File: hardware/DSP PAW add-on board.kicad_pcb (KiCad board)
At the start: 2 copper layers, 63 x 53.5 mm, 75 parts, among them J1 AudioJack2_Ground, J3 Conn_01x02, J4 Conn_02x03_Odd_Even, J5 AudioJack2_Ground, J7 AudioJack2_Ground, J8 USB_B_Micro, U1 TLV9162, U2 OPA1678, U3 MAX6106, U4 LM27761

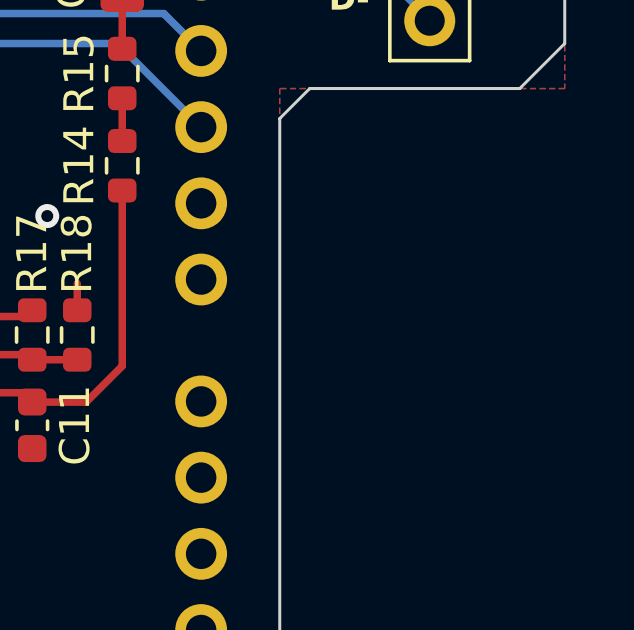
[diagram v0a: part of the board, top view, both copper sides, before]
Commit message: wip: schematic fixes based on testing
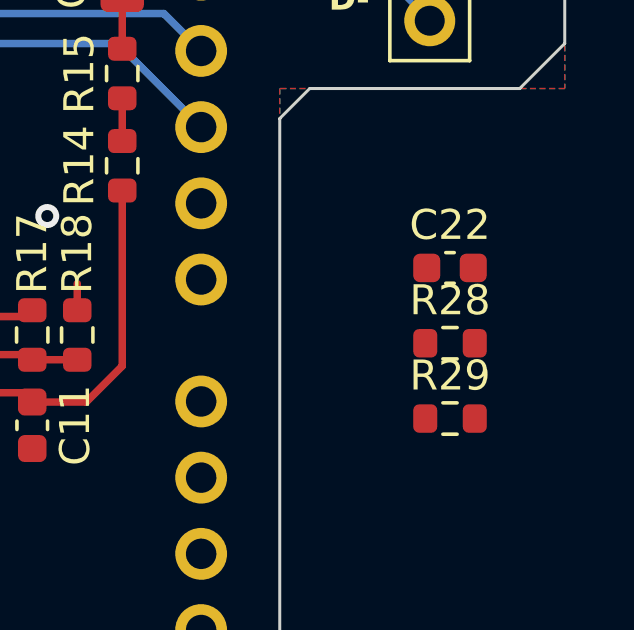
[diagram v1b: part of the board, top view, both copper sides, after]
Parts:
- added C22: 100p, Capacitor_SMD:C_0603_1608Metric, F.Cu at (179.2, 97.5)
- added R28: 100k, Resistor_SMD:R_0603_1608Metric, F.Cu at (179.2, 100.0)
- added R29: 100k, Resistor_SMD:R_0603_1608Metric, F.Cu at (179.2, 102.5)
- D1, D2, D3: value ESD5Zxx -> ESD5Z2.5T1G
- R1: value 9.09k -> 7.5k/0.1%
- R12, R13, R17, R18: value 2.49k -> 2.49k/0.1%
- R14, R8: value 22.1k -> 22.1k/0.1%
- R15, R9: value 6.81k -> 6.81k/0.1%
- R19: value 174k -> 174k/1%
- R21: value 56k -> 56k/1%
- R3: value 9.09k -> 9.09k/0.1%
- R4: value 6.34k -> 6.34k/0.1%
- R5: value 20k -> 10k/0.1%
- R7: value 10k/0.1% -> 30k/0.1%
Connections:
- net PC10/LED_R renamed LED_B
- net PC11/LED_G renamed LED_R
- net PC12/LED_B renamed LED_G
- A2 pad 5V1: +5VD -> VBUS
- A2 pad VIN: VBUS -> unconnected-(A2-PadVIN)
- C13 pad 1: +5VD -> VBUS
- C5 pad 2: Net-(U2A-+) -> Net-(C5-Pad2)
- C9 pad 2: Net-(U2B-+) -> Net-(C9-Pad2)
- L1 pad 1: +5VD -> VBUS
- R14 pad 2: Net-(R14-Pad2) -> Net-(C9-Pad2)
- R15 pad 1: Net-(R14-Pad2) -> Net-(C9-Pad2)
- R8 pad 2: Net-(R8-Pad2) -> Net-(C5-Pad2)
- R9 pad 1: Net-(R8-Pad2) -> Net-(C5-Pad2)
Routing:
- net Net-(R8-Pad2): track 1.50 -> 0.00 mm
- net Net-(C5-Pad2): track 0.00 -> 1.50 mm
- net Net-(R14-Pad2): track 1.42 -> 0.00 mm
- net Net-(C9-Pad2): track 0.00 -> 1.42 mm
- added copper zone on F.Cu, net VBUS
- removed copper zone on F.Cu, net +5VD

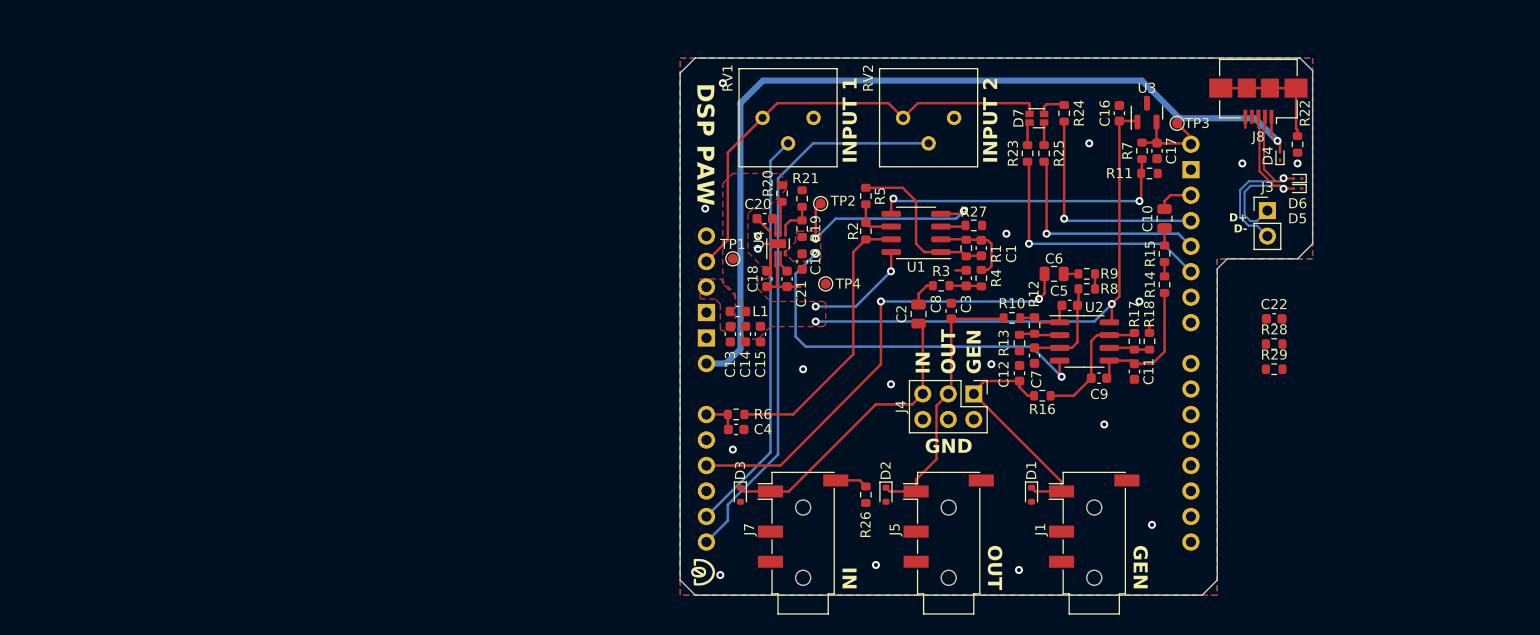
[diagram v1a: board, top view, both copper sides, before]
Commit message: use nucleo 3.3v vdda; add 2nd low-pass stage to input
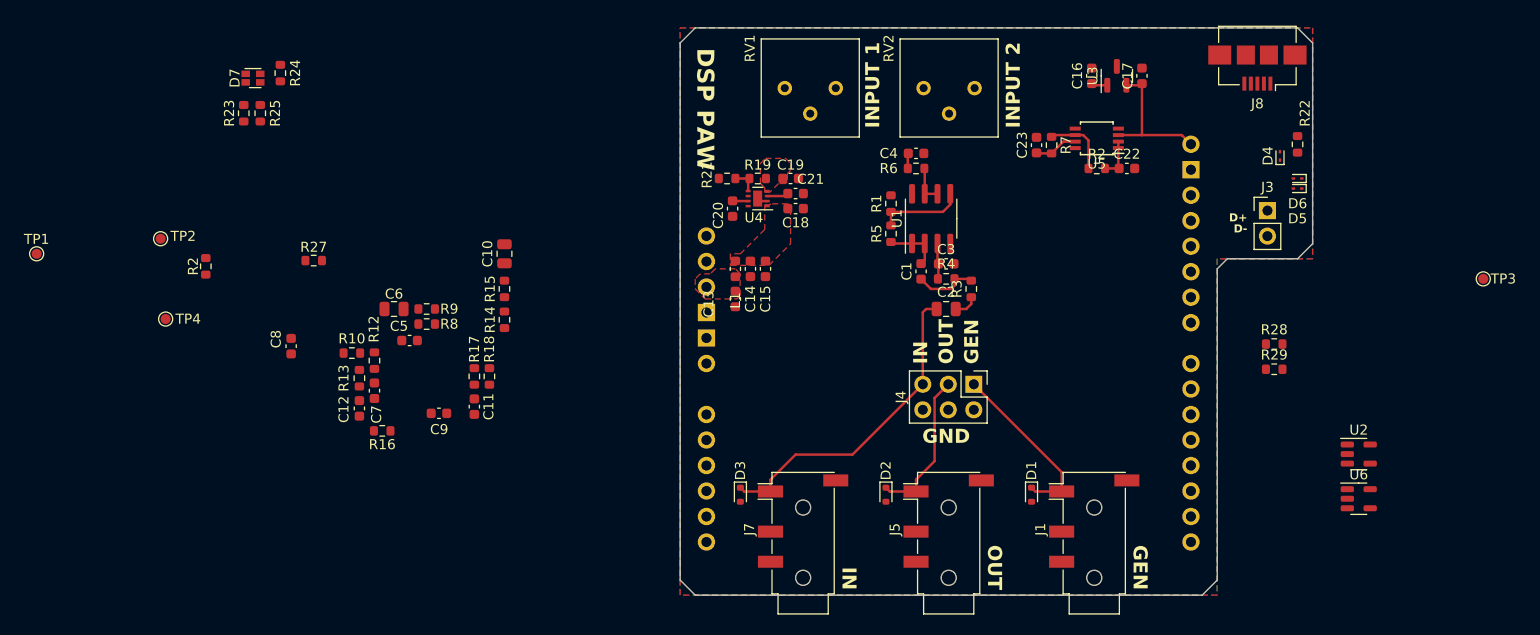
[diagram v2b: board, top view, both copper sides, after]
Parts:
- removed R11: 10k/0.1%, Resistor_SMD:R_0603_1608Metric
- removed R20, R26: 0, Resistor_SMD:R_0603_1608Metric
- added C23: 1u, Capacitor_SMD:C_0603_1608Metric, F.Cu at (155.5, 80.2)
- added R2: 10k/0.1%, Resistor_SMD:R_0603_1608Metric, F.Cu at (161.5, 82.5)
- added U5: OPA2310, Package_SO:TSSOP-8_3x3mm_P0.65mm, F.Cu at (161.5, 79.5)
- added U6: OPA1677, Package_TO_SOT_SMD:SOT-23-5, F.Cu at (187.6, 115.4)
- C1: value 100p -> 140p
- C22: value 100p -> 1u
- C3: value 274p -> 100p
- R1: value 7.5k/0.1% -> 10k/0.1%
- R3: value 9.09k/0.1% -> 8.45k/0.1%
- R4: value 6.34k/0.1% -> 13.2k/0.1%
- R7: value 30k/0.1% -> 10k/0.1%
- U2: value OPA1678 -> OPA1677; footprint Package_SO:SOIC-8_3.9x4.9mm_P1.27mm -> Package_TO_SOT_SMD:SOT-23-5
- U3: value MAX6106 -> REF3033
- moved D7 78.2 mm to (77.5, 73.5)
- moved R24 78.2 mm to (80.2, 73.0)
- moved R25 78.2 mm to (78.2, 77.0)
- moved R23 78.2 mm to (76.5, 77.0)
- moved TP1 69.4 mm to (55.9, 91.0)
- moved C12 65.8 mm to (88.0, 106.4)
- moved C5 65.8 mm to (93.0, 99.6)
- moved C7 65.8 mm to (89.5, 104.6)
- moved R10 65.8 mm to (87.3, 100.9)
- moved R12 65.8 mm to (89.5, 101.6)
- moved R13 65.8 mm to (88.0, 103.4)
- moved C10 65.8 mm to (102.5, 91.0)
- moved C11 65.8 mm to (99.5, 106.2)
- moved C6 65.8 mm to (91.5, 96.5)
- moved C8 65.8 mm to (81.2, 100.2)
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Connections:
- C1 pad 1: Net-(U1A--) -> Net-(C1-Pad1)
- C1 pad 2: Net-(C1-Pad2) -> Net-(U1A--)
- C11 pad 1: Net-(U2B-+) -> Net-(U6-+)
- C22 pad 1: Net-(U1B--) -> +3V3
- C22 pad 2: Net-(C22-Pad2) -> GND
- C3 pad 1: Net-(C3-Pad1) -> Net-(U1A-+)
- J7 pad S: Net-(J7-PadS) -> GND
- J8 pad 6: Net-(J8-Shield) -> GND
- R1 pad 1: Net-(U1A--) -> Net-(U1B-+)
- R1 pad 2: Net-(C1-Pad2) -> +3V3
- R12 pad 2: Net-(U2A--) -> Net-(U2--)
- R13 pad 1: Net-(U2A--) -> Net-(U2--)
- R14 pad 1: Net-(U2B-+) -> Net-(U6-+)
- R17 pad 2: Net-(U2B--) -> Net-(U6--)
- R18 pad 1: Net-(U2B--) -> Net-(U6--)
- R3 pad 2: Net-(C3-Pad1) -> Net-(C1-Pad1)
- R4 pad 1: Net-(C3-Pad1) -> Net-(C1-Pad1)
- R4 pad 2: Net-(U1A--) -> Net-(U1A-+)
- R5 pad 1: Net-(C1-Pad2) -> Net-(U1A--)
- R5 pad 2: Net-(U1B--) -> Net-(U1B-+)
- R6 pad 1: Net-(C22-Pad2) -> Net-(U1B--)
- R7 pad 1: VDDA/2 -> Net-(U5B--)
- R7 pad 2: VDDA -> -3V3
- RV1 pad 1: VCC -> +3V3
- RV2 pad 1: VCC -> +3V3
- U1 pad 1: Net-(C1-Pad2) -> Net-(U1A--)
- U1 pad 4: -5V -> -3V3
- U1 pad 5: VDDA/2 -> Net-(U1B-+)
- U1 pad 7: Net-(C22-Pad2) -> Net-(U1B--)
- U1 pad 8: +5V -> +3V3
- U2 pad 2: Net-(U2A--) -> -3V3
- U2 pad 4: -5V -> Net-(U2--)
- U2 pad 5: Net-(U2B-+) -> +3V3
- U4 pad 6: Net-(U4-EN) -> +5V
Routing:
- net VBUS: track 89.2 -> 0.00 mm, vias 1 -> 0
- net +5V: track 65.3 -> 1.62 mm, vias 4 -> 0
- net -5V: track 60.9 -> 0.00 mm, vias 4 -> 0
- net PC1/POT2: track 55.6 -> 0.00 mm
- net SIGNAL_OUT_MCU: track 46.4 -> 0.00 mm, vias 2 -> 0
- net VCC: track 46.1 -> 0.00 mm
- net PC0/POT1: track 40.5 -> 0.00 mm
- net VDDA/2: track 30.5 -> 0.00 mm, vias 2 -> 0
- net Net-(C22-Pad2): track 27.8 -> 0.00 mm
- net LED_B: track 25.5 -> 0.00 mm, vias 1 -> 0
- net LED_R: track 22.4 -> 0.00 mm, vias 1 -> 0
- net LED_G: track 22.2 -> 0.00 mm, vias 1 -> 0
- net USB_D_N: track 19.8 -> 0.00 mm, vias 1 -> 0
- net USB_D_P: track 19.1 -> 0.00 mm, vias 1 -> 0
- net Net-(C1-Pad2): track 16.8 -> 0.00 mm
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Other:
- board size 63 x 53.5 mm -> 63 x 56.5 mm

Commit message: finish rev2 layout
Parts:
- removed C16: 4.7u, Capacitor_SMD:C_0603_1608Metric
- removed C17: 1u, Capacitor_SMD:C_0603_1608Metric
- removed the R2 at (161.5, 82.5)
- removed R22, R27: 0, Resistor_SMD:R_0603_1608Metric
- removed U3: REF3033, Package_TO_SOT_SMD:SOT-23
- C4: value DNP -> 10n
- D7: footprint LED_SMD:LED_LiteOn_LTST-C19HE1WT -> LED_SMD:LED_Kingbright_AAA3528ESGCT
- R12, R13, R17, R18: value 2.49k/0.1% -> 2.49k/0.5%
- R14, R8: value 22.1k/0.1% -> 22.1k/0.5%
- R15, R9: value 6.81k/0.1% -> 6.81k/0.5%
- R3: value 8.45k/0.1% -> 8.45k/1%
- R4: value 13.2k/0.1% -> 13.3k/1%
- R6: value 0 -> 200
- moved R23 94.1 mm to (167.0, 103.0), turned to -90 degrees
- moved D7 93.6 mm to (165.0, 106.7), turned to 180 degrees
- moved R25 90.6 mm to (165.0, 103.0), turned to -90 degrees
- moved R24 88.1 mm to (163.0, 103.0), turned to -90 degrees
- moved R2 87.6 mm to (159.0, 77.0)
- moved TP3 76.2 mm to (126.0, 75.5)
- moved TP1 74.1 mm to (130.0, 90.0)
- moved R16 68.6 mm to (157.0, 92.7), turned to 90 degrees
- moved C12 67.7 mm to (154.5, 93.5), turned to 0 degrees
- moved C9 67.6 mm to (161.0, 88.5)
- moved TP2 66.7 mm to (134.5, 82.0)
- moved C11 65.4 mm to (161.0, 84.0), turned to 0 degrees
- moved C10 65.2 mm to (167.5, 85.5), turned to 0 degrees
- moved R15 62.3 mm to (164.2, 85.5), turned to 0 degrees
- moved TP4 60.3 mm to (126.0, 78.5)
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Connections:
- J1 pad R1: (no net) -> unconnected-(J1-PadR1)
- J1 pad R2: (no net) -> unconnected-(J1-PadR2)
- J5 pad R1: (no net) -> unconnected-(J5-PadR1)
- J5 pad R2: (no net) -> unconnected-(J5-PadR2)
- J7 pad R1: (no net) -> unconnected-(J7-PadR1)
- J7 pad R2: (no net) -> unconnected-(J7-PadR2)
- R2 pad 1: Net-(U1B--) -> Net-(U5B--)
- R2 pad 2: Net-(C22-Pad2) -> +3V3
- TP3 pad 1: VDDA -> +3V3
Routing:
- net +3V3: track 4.11 -> 97.2 mm, vias 0 -> 4
- net VCC: track 0.00 -> 85.0 mm, vias 0 -> 1
- net VBUS: track 0.00 -> 84.7 mm, vias 0 -> 2
- net -3V3: track 4.36 -> 76.4 mm, vias 0 -> 4
- net PC1/POT2: track 0.00 -> 62.1 mm
- net +5V: track 1.62 -> 49.2 mm, vias 0 -> 2
- net PC0/POT1: track 0.00 -> 46.9 mm
- net -5V: track 0.00 -> 37.5 mm, vias 0 -> 2
- net SIGNAL_IN_MCU: track 1.52 -> 35.9 mm
- net USB_D_N: track 0.00 -> 22.6 mm, vias 0 -> 1
- net USB_D_P: track 0.00 -> 21.9 mm, vias 0 -> 1
- net LED_R: track 0.00 -> 17.7 mm, vias 0 -> 1
- net GENERATOR: track 17.5 -> 34.4 mm
- net LED_G: track 0.00 -> 14.4 mm, vias 0 -> 1
- net SIGNAL_OUT: track 15.2 -> 27.7 mm, vias 0 -> 1
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
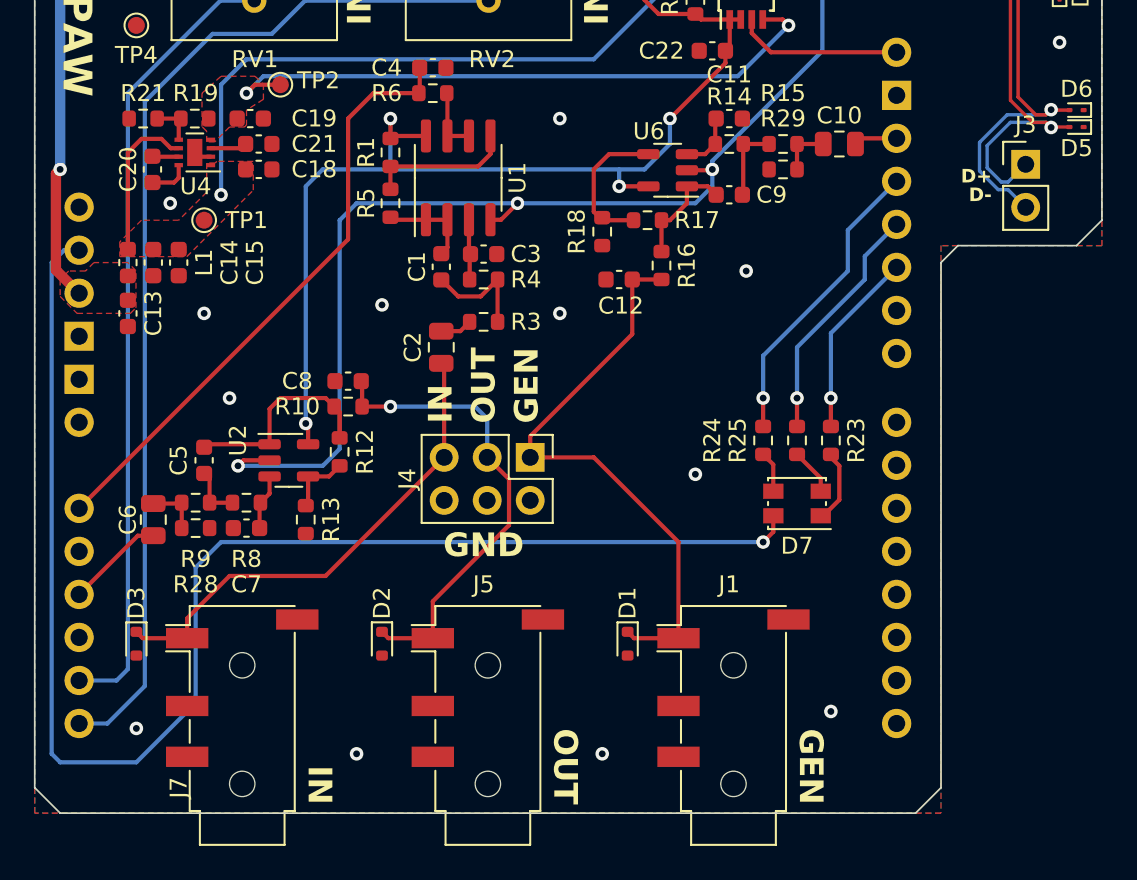
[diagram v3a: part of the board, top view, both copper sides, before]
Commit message: add 3d models back; flip USB data header
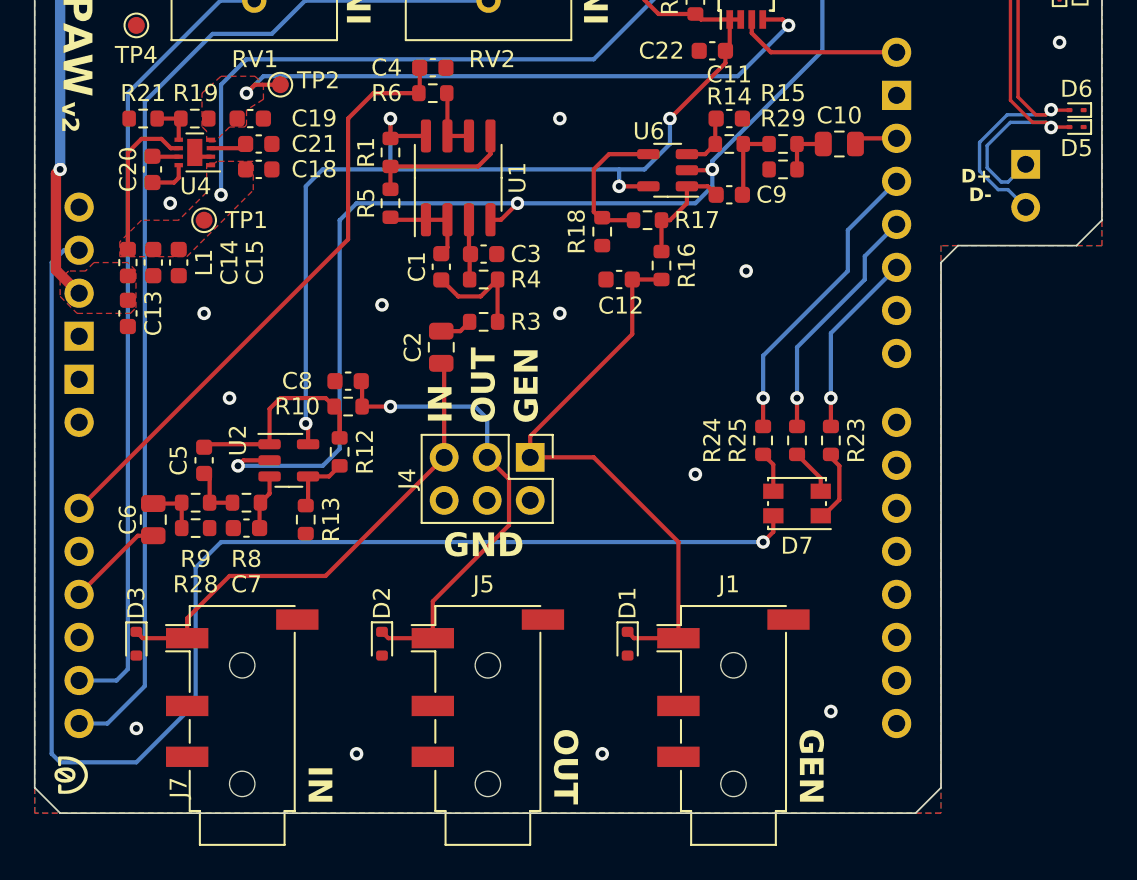
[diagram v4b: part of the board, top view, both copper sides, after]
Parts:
- J3: moved to B.Cu
- turned J3 to 180 degrees
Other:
- board text added: "v2"
